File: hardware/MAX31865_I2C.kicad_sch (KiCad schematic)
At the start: 38 parts, among them J1 Conn_01x08, J2 AVR-ISP-6, J3 Conn_02x04_Odd_Even, J4 Conn_02x04_Odd_Even, J5 Conn_02x02_Odd_Even, U1 ATmega48A-A, Y1 16MHz

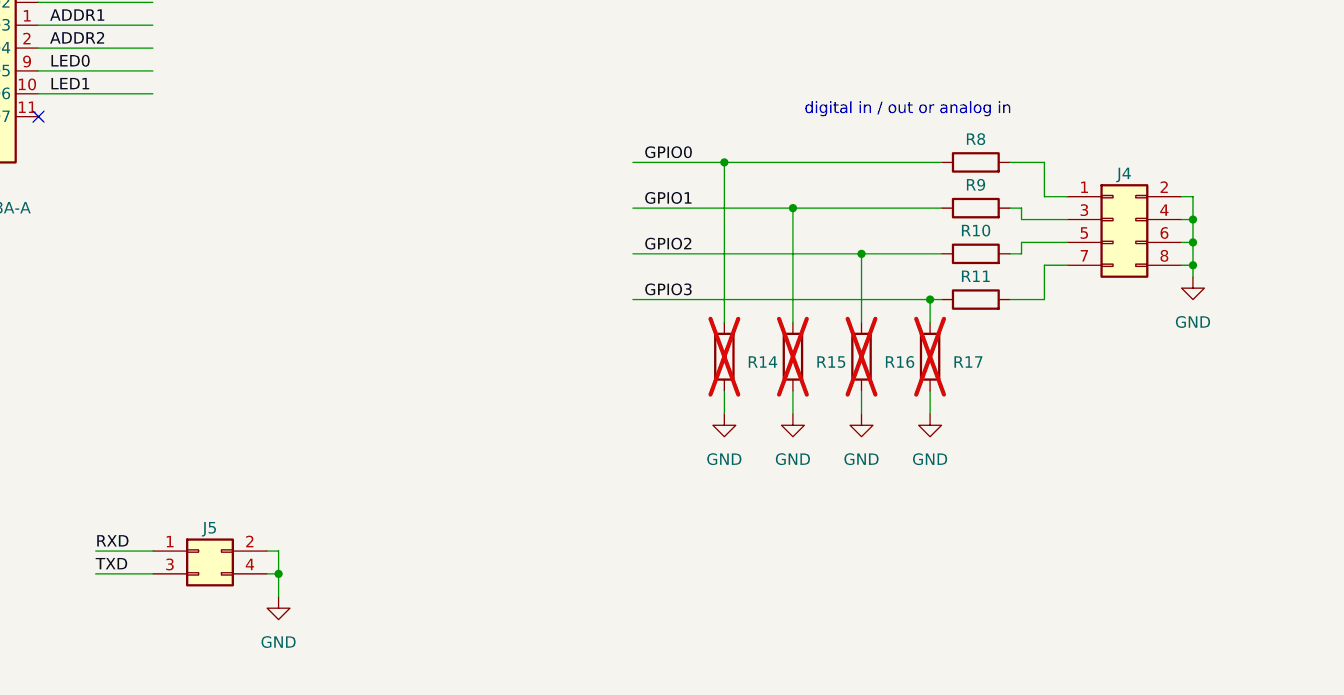
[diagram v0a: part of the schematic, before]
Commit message: fixed edge connectors for ISP
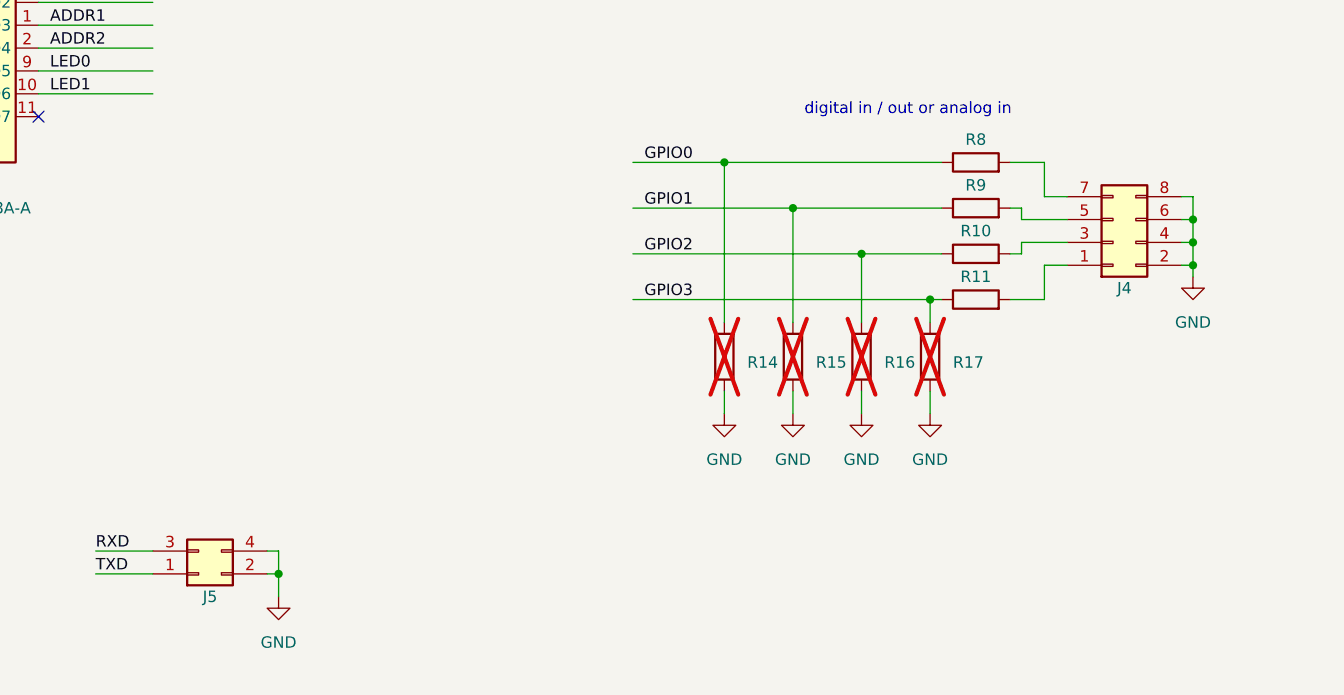
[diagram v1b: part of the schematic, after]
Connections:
- net RXD: now also J5.3 (Pin_3); no longer J5.1 (Pin_1)
- net TXD: now also J5.1 (Pin_1); no longer J5.3 (Pin_3)
- net at R10.2: now also J4.3 (Pin_3); no longer J4.5 (Pin_5)
- net at R8.2: now also J4.7 (Pin_7); no longer J4.1 (Pin_1)
- net at R11.2: now also J4.1 (Pin_1); no longer J4.7 (Pin_7)
- net at R9.2: now also J4.5 (Pin_5); no longer J4.3 (Pin_3)
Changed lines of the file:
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@@
     )
   )
-  (symbol (lib_id "Connector_Generic:Conn_02x02_Odd_Even") (at 80.01 168.91 0) (unit 1)
-    (in_bom yes) (on_board yes) (dnp no) (fields_autoplaced)
-    (property "Reference" "J5" (at 81.28 166.37 0)
-      (effects (font (size 1.27 1.27)))
-    )
-    (property "Value" "Conn_02x02_Odd_Even" (at 81.28 166.37 0)
-      (effects (font (size 1.27 1.27)) hide)
-    )
-    (property "Footprint" "PinHeaderEdgeMount:PinHeader_2x02_P2.54mm_Edge" (at 80.01 168.91 0)
-      (effects (font (size 1.27 1.27)) hide)
-    )
-    (property "Datasheet" "~" (at 80.01 168.91 0)
+  (symbol (lib_id "Connector_Generic:Conn_02x02_Odd_Even") (at 80.01 171.45 0) (mirror x) (unit 1)
+    (in_bom yes) (on_board yes) (dnp no)
+    (property "Reference" "J5" (at 81.28 173.99 0)
+      (effects (font (size 1.27 1.27)))
+    )
+    (property "Value" "Conn_02x02_Odd_Even" (at 81.28 173.99 0)
+      (effects (font (size 1.27 1.27)) hide)
+    )
+    (property "Footprint" "PinHeaderEdgeMount:PinHeader_2x02_P2.54mm_Edge" (at 80.01 171.45 0)
+      (effects (font (size 1.27 1.27)) hide)
+    )
+    (property "Datasheet" "~" (at 80.01 171.45 0)
       (effects (font (size 1.27 1.27)) hide)
     )
@@
     )
   )
-  (symbol (lib_id "Connector_Generic:Conn_02x04_Odd_Even") (at 181.61 132.08 0) (unit 1)
-    (in_bom yes) (on_board yes) (dnp no) (fields_autoplaced)
-    (property "Reference" "J4" (at 182.88 127 0)
-      (effects (font (size 1.27 1.27)))
-    )
-    (property "Value" "Conn_02x04_Odd_Even" (at 182.88 127 0)
-      (effects (font (size 1.27 1.27)) hide)
-    )
-    (property "Footprint" "PinHeaderEdgeMount:PinHeader_2x04_P2.54mm_Edge" (at 181.61 132.08 0)
-      (effects (font (size 1.27 1.27)) hide)
-    )
-    (property "Datasheet" "~" (at 181.61 132.08 0)
-      (effects (font (size 1.27 1.27)) hide)
-    )
+  (symbol (lib_id "Connector_Generic:Conn_02x04_Odd_Even") (at 181.61 134.62 0) (mirror x) (unit 1)
+    (in_bom yes) (on_board yes) (dnp no)
+    (property "Reference" "J4" (at 182.88 139.7 0)
+      (effects (font (size 1.27 1.27)))
+    )
+    (property "Value" "Conn_02x04_Odd_Even" (at 182.88 139.7 0)
+      (effects (font (size 1.27 1.27)) hide)
+    )
+    (property "Footprint" "PinHeaderEdgeMount:PinHeader_2x04_P2.54mm_Edge" (at 181.61 134.62 0)
+      (effects (font (size 1.27 1.27)) hide)
+    )
+    (property "Datasheet" "~" (at 181.61 134.62 0)
+      (effects (font (size 1.27 1.27)) hide)
+    )

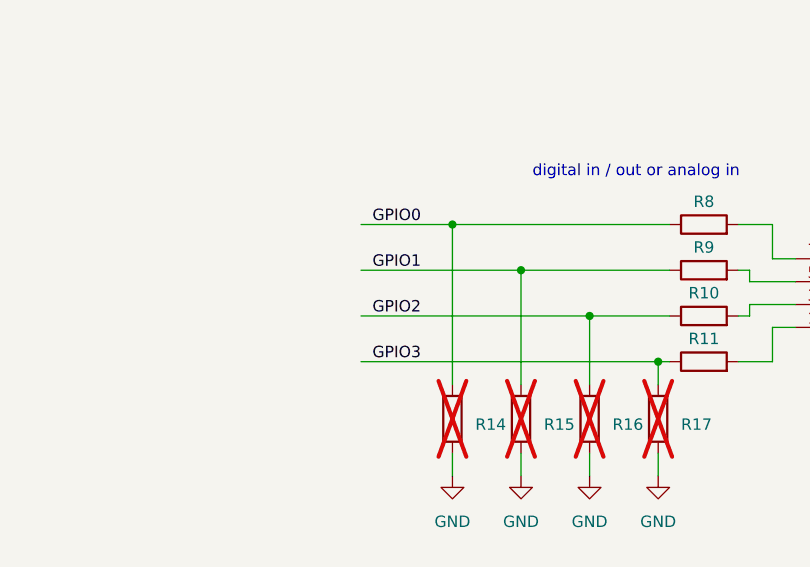
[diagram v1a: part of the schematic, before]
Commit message: GPIO input section redesign
Satisfies now the inner Monk
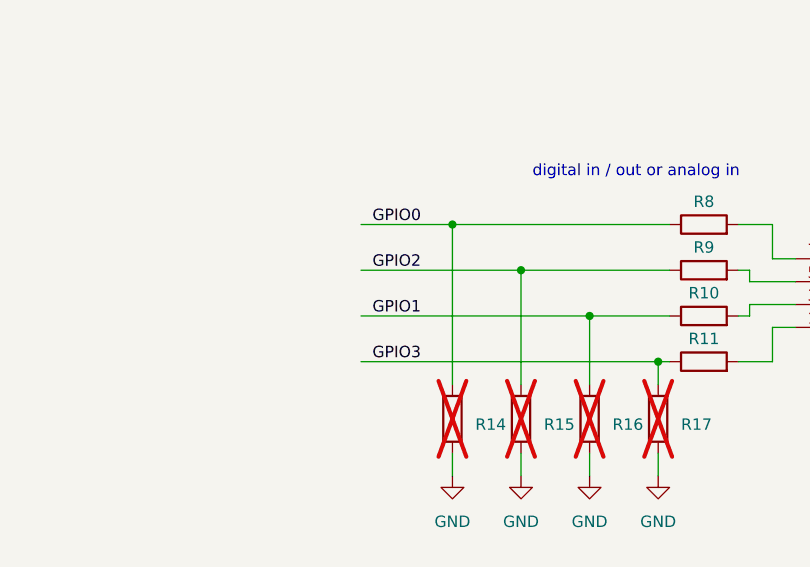
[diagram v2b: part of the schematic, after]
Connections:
- net GPIO1: now also R10.1, R16.2; no longer R15.2, R9.1
- net GPIO2: now also R15.2, R9.1; no longer R10.1, R16.2
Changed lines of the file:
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@@
     (effects (font (size 1.27 1.27)) (justify left bottom))
   )
-  (label "GPIO2" (at 129.54 135.89 0) (fields_autoplaced)
+  (label "GPIO2" (at 129.54 130.81 0) (fields_autoplaced)
     (effects (font (size 1.27 1.27)) (justify left bottom))
   )
@@
     (effects (font (size 1.27 1.27)) (justify left bottom))
   )
-  (label "GPIO1" (at 129.54 130.81 0) (fields_autoplaced)
-    (effects (font (size 1.27 1.27)) (justify left bottom))
-  )
   (label "VIN" (at 218.44 25.4 0) (fields_autoplaced)
     (effects (font (size 1.27 1.27)) (justify left bottom))
@@
     (effects (font (size 1.27 1.27)) (justify left bottom))
   )
+  (label "GPIO1" (at 129.54 135.89 0) (fields_autoplaced)
+    (effects (font (size 1.27 1.27)) (justify left bottom))
+  )

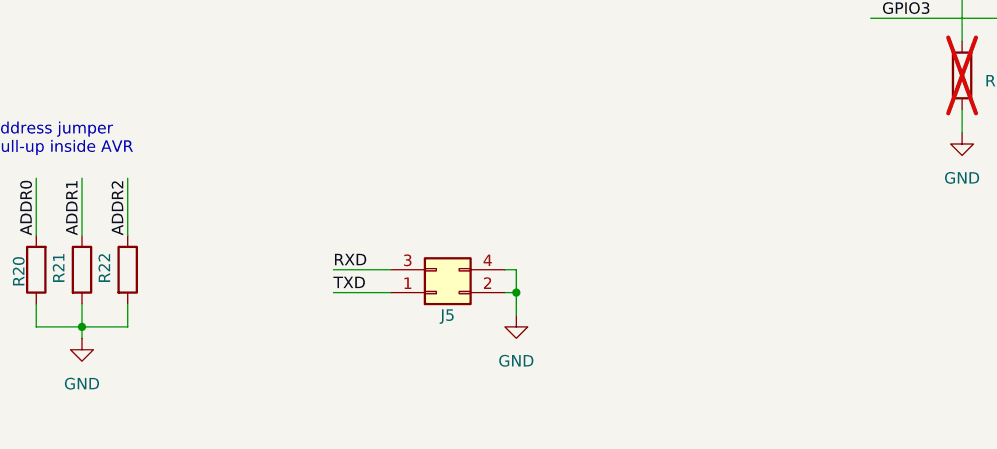
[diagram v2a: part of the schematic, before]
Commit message: added note about I2C address to schematic
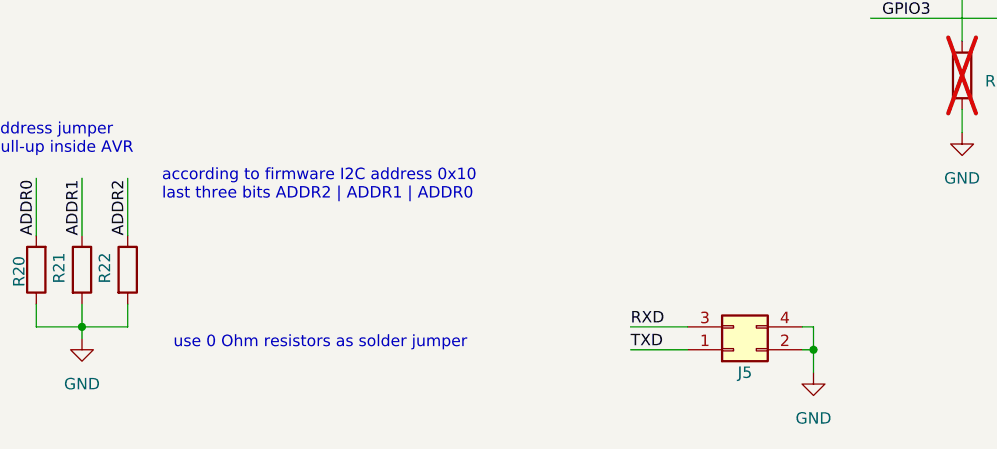
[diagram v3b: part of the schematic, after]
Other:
- note added: "according to firmware I2C address 0x10 last three bits ADDR2 | ADDR1 | ADDR0"
- note added: "use 0 Ohm resistors as solder jumper"
- moved on the sheet: J5
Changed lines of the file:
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@@
   (junction (at 138.43 125.73) (diameter 0) (color 0 0 0 0)
   )
-  (junction (at 88.9 171.45) (diameter 0) (color 0 0 0 0)
+  (junction (at 121.92 177.8) (diameter 0) (color 0 0 0 0)
   )
   (junction (at 99.06 88.9) (diameter 0) (color 0 0 0 0)
@@
     (stroke (width 0) (type default))
   )
-  (wire (pts (xy 68.58 168.91) (xy 74.93 168.91))
+  (wire (pts (xy 101.6 175.26) (xy 107.95 175.26))
     (stroke (width 0) (type default))
   )
@@
     (stroke (width 0) (type default))
   )
-  (wire (pts (xy 68.58 171.45) (xy 74.93 171.45))
+  (wire (pts (xy 101.6 177.8) (xy 107.95 177.8))
     (stroke (width 0) (type default))
   )
@@
     (stroke (width 0) (type default))
   )
-  (wire (pts (xy 87.63 168.91) (xy 88.9 168.91))
+  (wire (pts (xy 120.65 175.26) (xy 121.92 175.26))
     (stroke (width 0) (type default))
   )
@@
     (stroke (width 0) (type default))
   )
-  (wire (pts (xy 88.9 168.91) (xy 88.9 171.45))
+  (wire (pts (xy 121.92 175.26) (xy 121.92 177.8))
     (stroke (width 0) (type default))
   )
@@
     (stroke (width 0) (type default))
   )
-  (wire (pts (xy 88.9 171.45) (xy 88.9 173.99))
+  (wire (pts (xy 121.92 177.8) (xy 121.92 180.34))
     (stroke (width 0) (type default))
   )
@@
     (stroke (width 0) (type default))
   )
-  (wire (pts (xy 87.63 171.45) (xy 88.9 171.45))
+  (wire (pts (xy 120.65 177.8) (xy 121.92 177.8))
     (stroke (width 0) (type default))
   )
@@
     (effects (font (size 1.27 1.27)) (justify left bottom))
   )
+  (text "according to firmware I2C address 0x10\nlast three bits ADDR2 | ADDR1 | ADDR0"
+    (at 49.53 161.29 0)
+    (effects (font (size 1.27 1.27)) (justify left bottom))
+  )
   (text "AVR ISP Header" (at 254 78.74 0)
     (effects (font (size 1.27 1.27)) (justify left bottom))
@@
     (effects (font (size 1.27 1.27)) (justify left bottom))
   )
+  (text "use 0 Ohm resistors as solder jumper" (at 50.8 177.8 0)
+    (effects (font (size 1.27 1.27)) (justify left bottom))
+  )
   (label "SCK" (at 227.33 91.44 0) (fields_autoplaced)
     (effects (font (size 1.27 1.27)) (justify left bottom))
   )
-  (label "RXD" (at 68.58 168.91 0) (fields_autoplaced)
+  (label "RXD" (at 101.6 175.26 0) (fields_autoplaced)
     (effects (font (size 1.27 1.27)) (justify left bottom))
   )
@@
     (effects (font (size 1.27 1.27)) (justify left bottom))
   )
-  (label "TXD" (at 68.58 171.45 0) (fields_autoplaced)
+  (label "TXD" (at 101.6 177.8 0) (fields_autoplaced)
     (effects (font (size 1.27 1.27)) (justify left bottom))
   )
@@
     )
   )
-  (symbol (lib_id "Connector_Generic:Conn_02x02_Odd_Even") (at 80.01 171.45 0) (mirror x) (unit 1)
+  (symbol (lib_id "Connector_Generic:Conn_02x02_Odd_Even") (at 113.03 177.8 0) (mirror x) (unit 1)
     (in_bom yes) (on_board yes) (dnp no)
-    (property "Reference" "J5" (at 81.28 173.99 0)
-      (effects (font (size 1.27 1.27)))
-    )
-    (property "Value" "Conn_02x02_Odd_Even" (at 81.28 173.99 0)
-      (effects (font (size 1.27 1.27)) hide)
-    )
-    (property "Footprint" "PinHeaderEdgeMount:PinHeader_2x02_P2.54mm_Edge" (at 80.01 171.45 0)
-      (effects (font (size 1.27 1.27)) hide)
-    )
-    (property "Datasheet" "~" (at 80.01 171.45 0)
+    (property "Reference" "J5" (at 114.3 180.34 0)
+      (effects (font (size 1.27 1.27)))
+    )
+    (property "Value" "Conn_02x02_Odd_Even" (at 114.3 180.34 0)
+      (effects (font (size 1.27 1.27)) hide)
+    )
+    (property "Footprint" "PinHeaderEdgeMount:PinHeader_2x02_P2.54mm_Edge" (at 113.03 177.8 0)
+      (effects (font (size 1.27 1.27)) hide)
+    )
+    (property "Datasheet" "~" (at 113.03 177.8 0)
       (effects (font (size 1.27 1.27)) hide)
     )
@@
     )
   )
-  (symbol (lib_id "PCM_4ms_Power-symbol:GND") (at 88.9 173.99 0) (unit 1)
-    (in_bom yes) (on_board yes) (dnp no) (fields_autoplaced)
-    (property "Reference" "#PWR030" (at 88.9 180.34 0)
-      (effects (font (size 1.27 1.27)) hide)
-    )
-    (property "Value" "GND" (at 88.9 179.07 0)
-      (effects (font (size 1.27 1.27)))
-    )
-    (property "Footprint" "" (at 88.9 173.99 0)
-      (effects (font (size 1.27 1.27)) hide)
-    )
-    (property "Datasheet" "" (at 88.9 173.99 0)
-      (effects (font (size 1.27 1.27)) hide)
-    )
+  (symbol (lib_id "PCM_4ms_Power-symbol:GND") (at 121.92 180.34 0) (unit 1)
+    (in_bom yes) (on_board yes) (dnp no) (fields_autoplaced)
+    (property "Reference" "#PWR030" (at 121.92 186.69 0)
+      (effects (font (size 1.27 1.27)) hide)
+    )
+    (property "Value" "GND" (at 121.92 185.42 0)
+      (effects (font (size 1.27 1.27)))
+    )
+    (property "Footprint" "" (at 121.92 180.34 0)
+      (effects (font (size 1.27 1.27)) hide)
+    )
+    (property "Datasheet" "" (at 121.92 180.34 0)
+      (effects (font (size 1.27 1.27)) hide)
+    )
